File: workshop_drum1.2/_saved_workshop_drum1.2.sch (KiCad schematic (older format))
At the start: 35 parts, among them J1 9v, J2 INPUT, J3 OUTPUT, SW1 POWER, SW2 OSCILLATOR SELECT, SW3 BUTTON, U1 LM358, U2 7414, U3 78L05

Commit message: Made PCB look cool - but havent updated from sch yet
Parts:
- LOGO3: footprint zfoot:Logo_OSH-2 -> zfoot:Logo_OSH-3
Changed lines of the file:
@@
 U 1 1 5A33DD61
 P 5950 1850
-F 0 "BreadBoardStrip1" H 6000 2000 60  0000 C CNN
+F 0 "BreadBoardStrip1" H 6150 1650 60  0001 C CNN
 F 1 "Path to Switch" H 6009 1795 10  0000 C CNN
 F 2 "zfoot:BREAKOUTswitch" H 5820 1830 60  0001 C CNN
@@
 F 0 "LOGO3" H 6715 4096 50  0000 L CNN
 F 1 "OSH" H 6715 4005 50  0000 L CNN
-F 2 "zfoot:Logo_OSH-2" H 6638 3900 50  0001 C CNN
+F 2 "zfoot:Logo_OSH-3" H 6638 3900 50  0001 C CNN
 F 3 "" H 6600 4050 50  0001 C CNN
 	1    6600 4050

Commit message: Ordered v1.2 - generated gerbers and arranged artwork
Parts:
- added LOGO4: OSC, zfoot:Logo_OSC-1, symbol zMECH:Logo
- added LOGO5: MNT, zfoot:Logo_MNT-2, symbol zMECH:Logo
- LOGO1: footprint zfoot:Logo_Open-1 -> zfoot:Logo_Open-3; symbol 4ms-passives:C -> zMECH:Logo
- LOGO2, LOGO3: symbol 4ms-passives:C -> zMECH:Logo
- SW1: footprint zfoot:Switch_Toggle_SPST_Mini_SolderLug_2legs -> zfoot:Switch_Toggle_SPST_Mini_SolderLug_2legs_Circle
- SW2: footprint zfoot:Switch_Toggle_SPDT_Mini_SolderLug -> zfoot:Switch_Toggle_SPDT_Mini_SolderLug_Circle
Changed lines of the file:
@@
 F 0 "SW2" H 6000 1750 60  0000 C CNN
 F 1 "OSCILLATOR SELECT" H 6100 2060 20  0000 C CNN
-F 2 "zfoot:Switch_Toggle_SPDT_Mini_SolderLug" H 6100 1900 60  0001 C CNN
+F 2 "zfoot:Switch_Toggle_SPDT_Mini_SolderLug_Circle" H 6100 1900 60  0001 C CNN
 F 3 "" H 6100 1900 60  0001 C CNN
 	1    6100 1900
@@
 F 0 "SW1" H 1800 3484 60  0000 C CNN
 F 1 "POWER" H 1800 3410 20  0000 C CNN
-F 2 "zfoot:Switch_Toggle_SPST_Mini_SolderLug_2legs" H 1800 3250 60  0001 C CNN
+F 2 "zfoot:Switch_Toggle_SPST_Mini_SolderLug_2legs_Circle" H 1800 3250 60  0001 C CNN
 F 3 "" H 1800 3250 60  0001 C CNN
 	1    1800 3250
@@
 	5500 1950 5500 2500
 $Comp
-L 4ms-passives:C LOGO1
+L zMECH:Logo LOGO1
 U 1 1 5ADBC7A3
-P 5800 4050
-F 0 "LOGO1" H 5915 4096 50  0000 L CNN
-F 1 "Open" H 5915 4005 50  0000 L CNN
-F 2 "zfoot:Logo_Open-1" H 5838 3900 50  0001 C CNN
-F 3 "" H 5800 4050 50  0001 C CNN
-	1    5800 4050
-	1    0    0    -1
-$EndComp
-$Comp
-L 4ms-passives:C LOGO2
+P 5550 3900
+F 0 "LOGO1" H 5673 3945 50  0000 L CNN
+F 1 "Open" H 5673 3854 50  0000 L CNN
+F 2 "zfoot:Logo_Open-3" H 5588 3750 50  0001 C CNN
+F 3 "" H 5550 3900 50  0001 C CNN
+	1    5550 3900
+	1    0    0    -1
+$EndComp
+$Comp
+L zMECH:Logo LOGO2
 U 1 1 5ADBC845
-P 6150 4000
-F 0 "LOGO2" H 6265 4046 50  0000 L CNN
-F 1 "S1" H 6265 3955 50  0000 L CNN
-F 2 "zfoot:Logo_S1-2" H 6188 3850 50  0001 C CNN
-F 3 "" H 6150 4000 50  0001 C CNN
-	1    6150 4000
-	1    0    0    -1
-$EndComp
-$Comp
-L 4ms-passives:C LOGO3
+P 6050 3900
+F 0 "LOGO2" H 6173 3945 50  0000 L CNN
+F 1 "S1" H 6173 3854 50  0000 L CNN
+F 2 "zfoot:Logo_S1-2" H 6088 3750 50  0001 C CNN
+F 3 "" H 6050 3900 50  0001 C CNN
+	1    6050 3900
+	1    0    0    -1
+$EndComp
+$Comp
+L zMECH:Logo LOGO3
 U 1 1 5ADBC8AF
-P 6600 4050
-F 0 "LOGO3" H 6715 4096 50  0000 L CNN
-F 1 "OSH" H 6715 4005 50  0000 L CNN
-F 2 "zfoot:Logo_OSH-3" H 6638 3900 50  0001 C CNN
-F 3 "" H 6600 4050 50  0001 C CNN
-	1    6600 4050
-	1    0    0    -1
-$EndComp
+P 6500 3900
+F 0 "LOGO3" H 6623 3945 50  0000 L CNN
+F 1 "OSH" H 6623 3854 50  0000 L CNN
+F 2 "zfoot:Logo_OSH-3" H 6538 3750 50  0001 C CNN
+F 3 "" H 6500 3900 50  0001 C CNN
+	1    6500 3900
+	1    0    0    -1
+$EndComp
+$Comp
+L zMECH:Logo LOGO4
+U 1 1 5ADD0544
+P 6950 3900
+F 0 "LOGO4" H 7073 3945 50  0000 L CNN
+F 1 "OSC" H 7073 3854 50  0000 L CNN
+F 2 "zfoot:Logo_OSC-1" H 6988 3750 50  0001 C CNN
+F 3 "" H 6950 3900 50  0001 C CNN
+	1    6950 3900
+	1    0    0    -1
+$EndComp
+$Comp
+L zMECH:Logo LOGO5
+U 1 1 5ADD05B6
+P 7400 3900
+F 0 "LOGO5" H 7523 3945 50  0000 L CNN
+F 1 "MNT" H 7523 3854 50  0000 L CNN
+F 2 "zfoot:Logo_MNT-2" H 7438 3750 50  0001 C CNN
+F 3 "" H 7400 3900 50  0001 C CNN
+	1    7400 3900
+	1    0    0    -1
+$EndComp

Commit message: redid silk - this is the one sent to OSH 5/4/18
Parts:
- LOGO2: footprint zfoot:Logo_S1-2 -> zfoot:S1SMalllllllaf
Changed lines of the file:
@@
 F 0 "LOGO2" H 6173 3945 50  0000 L CNN
 F 1 "S1" H 6173 3854 50  0000 L CNN
-F 2 "zfoot:Logo_S1-2" H 6088 3750 50  0001 C CNN
+F 2 "zfoot:S1SMalllllllaf" H 6088 3750 50  0001 C CNN
 F 3 "" H 6050 3900 50  0001 C CNN
 	1    6050 3900

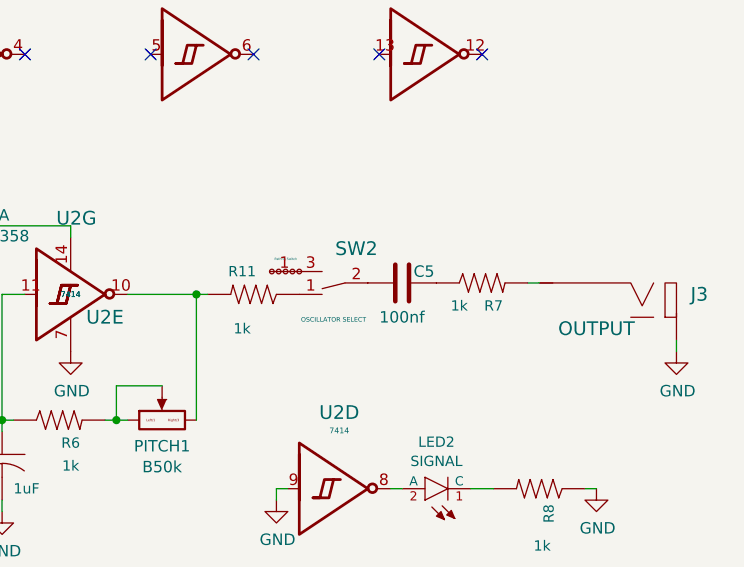
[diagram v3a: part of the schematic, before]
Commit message: changed C5 from 100nf to 1uF - ceramic to elect cap - generated grbs
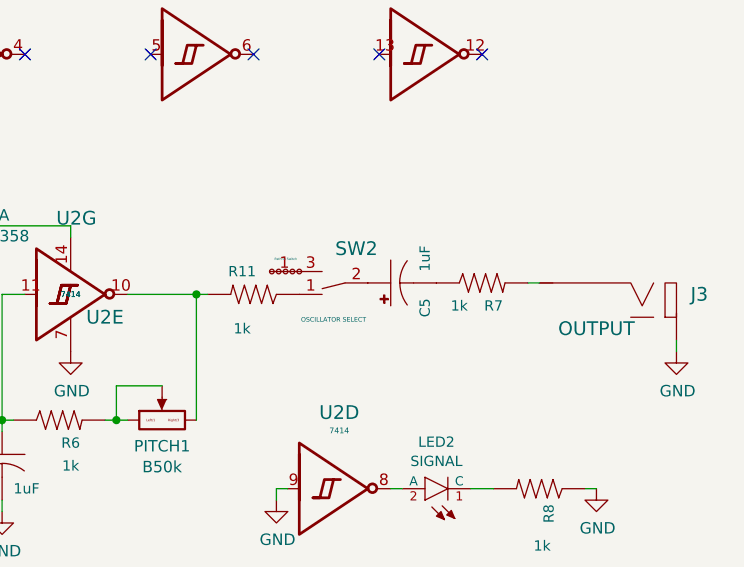
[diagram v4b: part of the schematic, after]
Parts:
- removed C5: 100nf, 4ms-footprints:Cap_Ceramic_TH, symbol 4ms-passives:CAP_TH
- added C5: 1uF, 4ms-footprints:Cap_Electrolytic_TH, symbol 4ms-passives:CAP-ELEC-TH
- LOGO3: footprint zfoot:Logo_OSH-3 -> zfoot:Logo_OSH-4
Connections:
- net at R7.1: now also C5.2 (-)
- net at SW2.2: now also C5.1 (+)
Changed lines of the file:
@@
-$EndComp
-$Comp
-L 4ms-passives:CAP_TH C5
-U 1 1 5A3339E6
-P 6400 1900
-F 0 "C5" V 6350 1950 50  0000 L CNN
-F 1 "100nf" V 6550 1800 50  0000 L CNN
-F 2 "4ms-footprints:Cap_Ceramic_TH" H 6438 1750 50  0001 C CNN
-F 3 "" H 6400 1900 50  0001 C CNN
-	1    6400 1900
-	0    1    1    0
 $EndComp
 $Comp
@@
 F 0 "LOGO3" H 6623 3945 50  0000 L CNN
 F 1 "OSH" H 6623 3854 50  0000 L CNN
-F 2 "zfoot:Logo_OSH-3" H 6538 3750 50  0001 C CNN
+F 2 "zfoot:Logo_OSH-4" H 6538 3750 50  0001 C CNN
 F 3 "" H 6500 3900 50  0001 C CNN
 	1    6500 3900
@@
 	1    0    0    -1
 $EndComp
+$Comp
+L 4ms-passives:CAP-ELEC-TH C5
+U 1 1 5AEF6818
+P 6350 1900
+F 0 "C5" H 6200 1750 45  0000 L CNN
+F 1 "1uF" H 6400 1750 45  0000 L CNN
+F 2 "4ms-footprints:Cap_Electrolytic_TH" H 6380 2050 20  0001 C CNN
+F 3 "" H 6350 1900 60  0001 C CNN
+	1    6350 1900
+	0    -1   -1   0
+$EndComp
 $EndSCHEMATC
